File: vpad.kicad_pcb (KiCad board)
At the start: 2 copper layers, 100.6 x 109.4 mm, 53 parts, among them J1 Conn_01x10_Socket, J2 Conn_01x10_Socket, SW1 SW_Push_45deg, SW10 SW_Push_45deg, SW11 SW_Push_45deg, SW12 SW_Push_45deg, SW13 SW_Push_45deg, SW14 SW_Push_45deg, SW15 SW_Push_45deg, SW16 SW_Push_45deg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

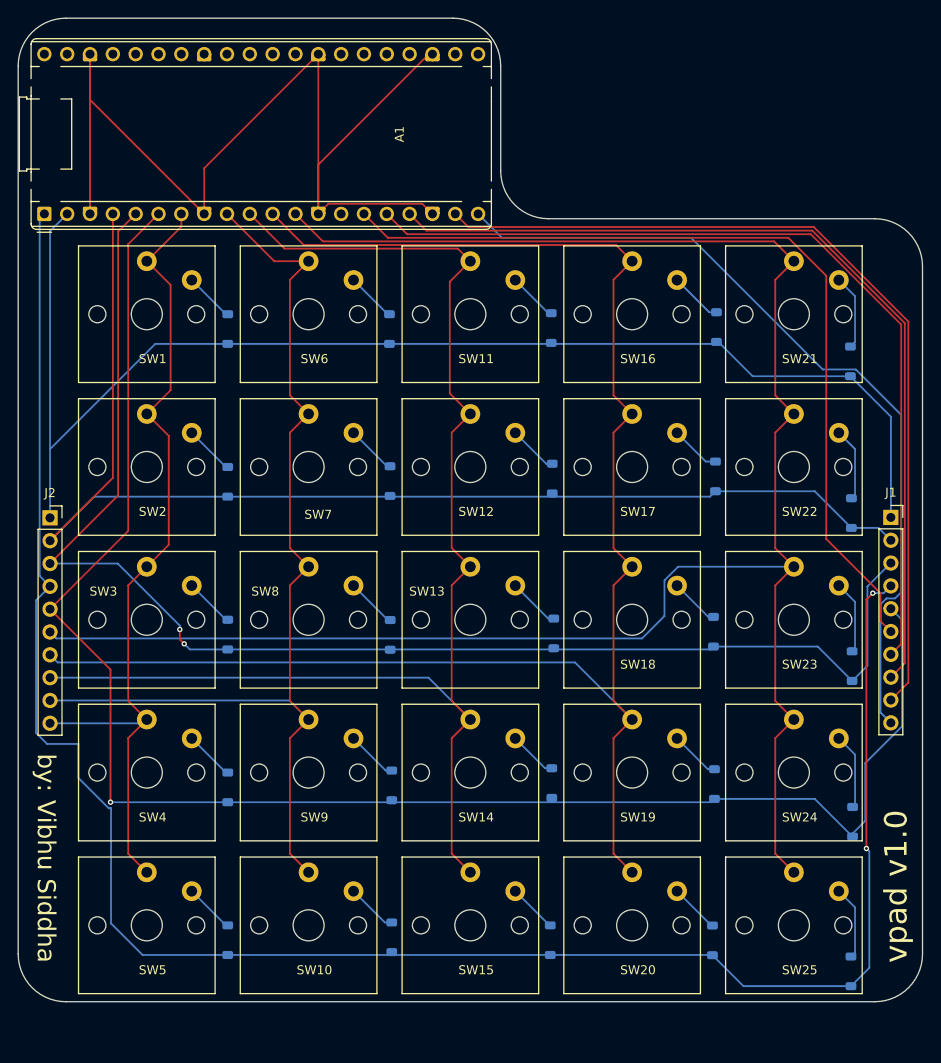
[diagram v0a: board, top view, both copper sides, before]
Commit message: added mounting holes
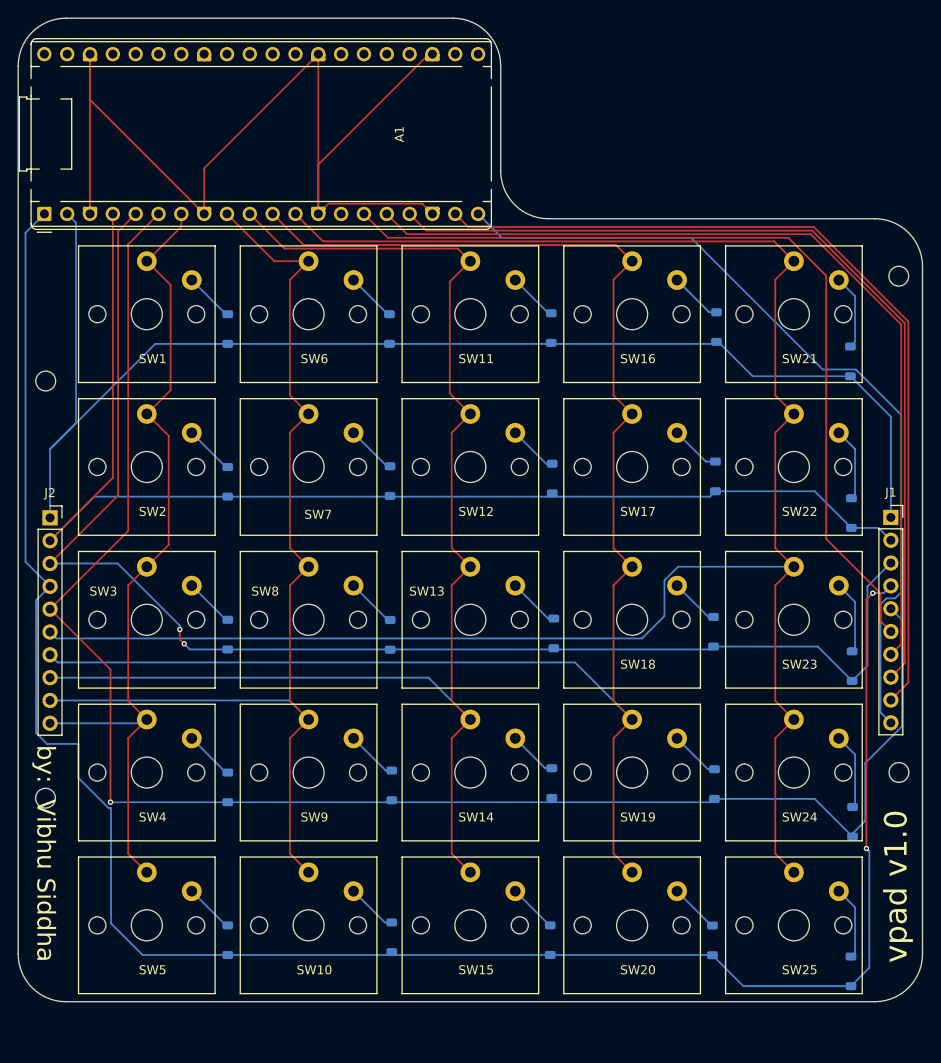
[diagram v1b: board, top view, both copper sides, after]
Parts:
- added H1: MountingHole, MountingHole:MountingHole_2.2mm_M2, B.Cu at (51.4, 68.3)
- added H2: MountingHole, MountingHole:MountingHole_2.2mm_M2, B.Cu at (51.4, 114.7)
- added H3: MountingHole, MountingHole:MountingHole_2.2mm_M2, B.Cu at (146.3, 56.6)
- added H4: MountingHole, MountingHole:MountingHole_2.2mm_M2, B.Cu at (146.3, 111.9)
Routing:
- net ROW5: track 218.5 -> 219.8 mm
- net ROW1: track 147.8 -> 148.6 mm

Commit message: edited mounting to m3, added case
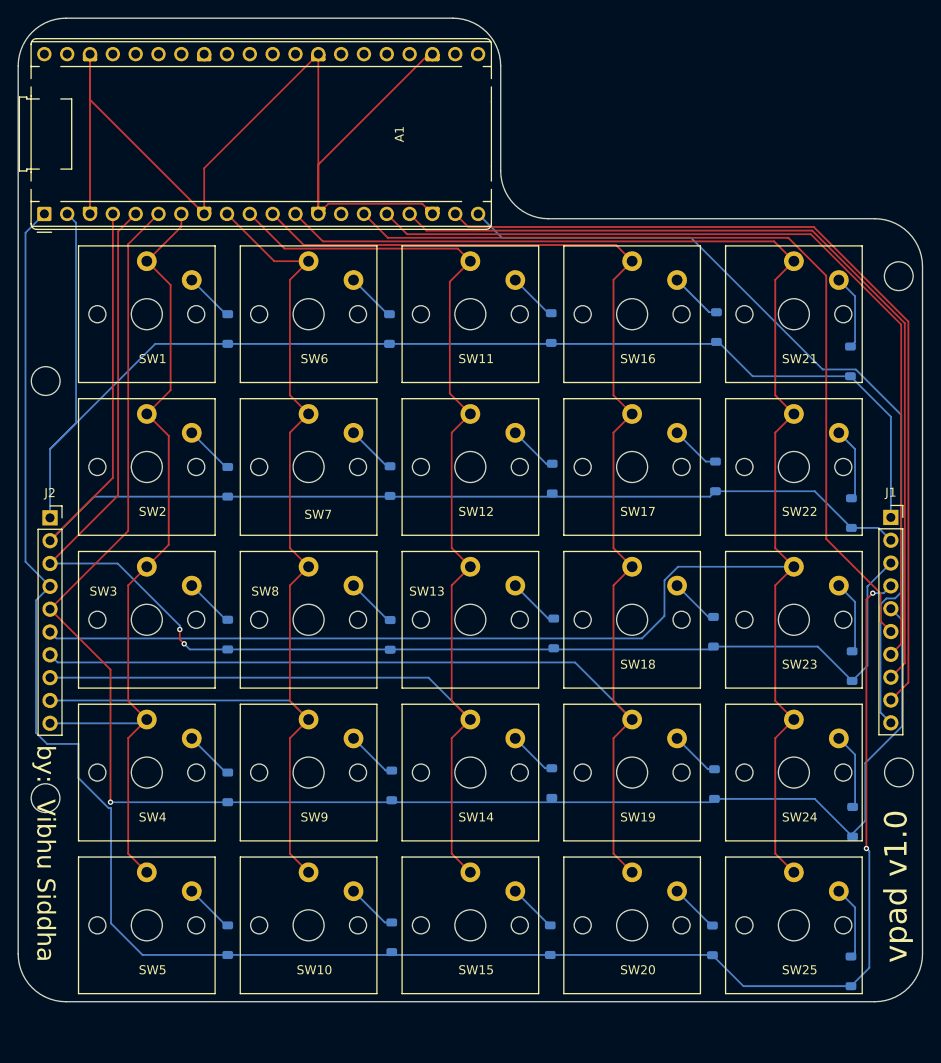
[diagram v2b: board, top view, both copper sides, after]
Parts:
- H1, H2, H3, H4: footprint MountingHole:MountingHole_2.2mm_M2 -> MountingHole:MountingHole_3.2mm_M3
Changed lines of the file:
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@@
 		)
 	)
-	(footprint "MountingHole:MountingHole_2.2mm_M2"
+	(footprint "MountingHole:MountingHole_3.2mm_M3"
 		(layer "B.Cu")
 		(at 51.41 68.3025)
-		(descr "Mounting Hole 2.2mm, M2, no annular, generated by kicad-footprint-generator mountinghole.py")
-		(tags "mountinghole M2")
+		(descr "Mounting Hole 3.2mm, M3, no annular, generated by kicad-footprint-generator mountinghole.py")
+		(tags "mountinghole M3")
 		(property "Reference" "H1"
-			(at 0 3.15 180)
+			(at 0 4.15 180)
 			(layer "B.SilkS")
 			(effects
@@
 		)
 		(property "Value" "MountingHole"
-			(at 0 -3.15 180)
+			(at 0 -4.15 180)
 			(layer "B.Fab")
 			(hide yes)
@@
 		(fp_circle
 			(center 0 0)
-			(end 2.2 0)
+			(end 3.2 0)
 			(stroke
 				(width 0.15)
@@
 		(fp_circle
 			(center 0 0)
-			(end 2.45 0)
+			(end 3.45 0)
 			(stroke
 				(width 0.05)
@@
 		(pad "" np_thru_hole circle
 			(at 0 0)
-			(size 2.2 2.2)
-			(drill 2.2)
+			(size 3.2 3.2)
+			(drill 3.2)
 			(layers "*.Cu" "*.Mask")
 		)
@@
 		)
 	)
-	(footprint "MountingHole:MountingHole_2.2mm_M2"
+	(footprint "MountingHole:MountingHole_3.2mm_M3"
 		(layer "B.Cu")
 		(at 51.39 114.715)
-		(descr "Mounting Hole 2.2mm, M2, no annular, generated by kicad-footprint-generator mountinghole.py")
-		(tags "mountinghole M2")
+		(descr "Mounting Hole 3.2mm, M3, no annular, generated by kicad-footprint-generator mountinghole.py")
+		(tags "mountinghole M3")
 		(property "Reference" "H2"
-			(at 0 3.15 180)
+			(at 0 4.15 180)
 			(layer "B.SilkS")
 			(effects
@@
 		)
 		(property "Value" "MountingHole"
-			(at 0 -3.15 180)
+			(at 0 -4.15 180)
 			(layer "B.Fab")
 			(hide yes)
@@
 		(fp_circle
 			(center 0 0)
-			(end 2.2 0)
+			(end 3.2 0)
 			(stroke
 				(width 0.15)
@@
 		(fp_circle
 			(center 0 0)
-			(end 2.45 0)
+			(end 3.45 0)
 			(stroke
 				(width 0.05)
@@
 		(pad "" np_thru_hole circle
 			(at 0 0)
-			(size 2.2 2.2)
-			(drill 2.2)
+			(size 3.2 3.2)
+			(drill 3.2)
 			(layers "*.Cu" "*.Mask")
 		)
@@
 		)
 	)
-	(footprint "MountingHole:MountingHole_2.2mm_M2"
+	(footprint "MountingHole:MountingHole_3.2mm_M3"
 		(layer "B.Cu")
 		(at 146.35 111.855)
-		(descr "Mounting Hole 2.2mm, M2, no annular, generated by kicad-footprint-generator mountinghole.py")
-		(tags "mountinghole M2")
+		(descr "Mounting Hole 3.2mm, M3, no annular, generated by kicad-footprint-generator mountinghole.py")
+		(tags "mountinghole M3")
 		(property "Reference" "H4"
-			(at 0 3.15 180)
+			(at 0 4.15 180)
 			(layer "B.SilkS")
 			(effects
@@
 		)
 		(property "Value" "MountingHole"
-			(at 0 -3.15 180)
+			(at 0 -4.15 180)
 			(layer "B.Fab")
 			(hide yes)
@@
 		(fp_circle
 			(center 0 0)
-			(end 2.2 0)
+			(end 3.2 0)
 			(stroke
 				(width 0.15)
@@
 		(fp_circle
 			(center 0 0)
-			(end 2.45 0)
+			(end 3.45 0)
 			(stroke
 				(width 0.05)
@@
 		(pad "" np_thru_hole circle
 			(at 0 0)
-			(size 2.2 2.2)
-			(drill 2.2)
+			(size 3.2 3.2)
+			(drill 3.2)
 			(layers "*.Cu" "*.Mask")
 		)
@@
 		)
 	)
-	(footprint "MountingHole:MountingHole_2.2mm_M2"
+	(footprint "MountingHole:MountingHole_3.2mm_M3"
 		(layer "B.Cu")
 		(at 146.33 56.635)
-		(descr "Mounting Hole 2.2mm, M2, no annular, generated by kicad-footprint-generator mountinghole.py")
-		(tags "mountinghole M2")
+		(descr "Mounting Hole 3.2mm, M3, no annular, generated by kicad-footprint-generator mountinghole.py")
+		(tags "mountinghole M3")
 		(property "Reference" "H3"
-			(at 0 3.15 180)
+			(at 0 4.15 180)
 			(layer "B.SilkS")
 			(effects
@@
 		)
 		(property "Value" "MountingHole"
-			(at 0 -3.15 180)
+			(at 0 -4.15 180)
 			(layer "B.Fab")
 			(hide yes)
@@
 		(fp_circle
 			(center 0 0)
-			(end 2.2 0)
+			(end 3.2 0)
 			(stroke
 				(width 0.15)
@@
 		(fp_circle
 			(center 0 0)
-			(end 2.45 0)
+			(end 3.45 0)
 			(stroke
 				(width 0.05)
@@
 		(pad "" np_thru_hole circle
 			(at 0 0)
-			(size 2.2 2.2)
-			(drill 2.2)
+			(size 3.2 3.2)
+			(drill 3.2)
 			(layers "*.Cu" "*.Mask")
 		)
